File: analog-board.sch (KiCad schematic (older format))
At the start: 488 parts, among them J1 AC IN, J2 OUT, J3 CONN_20X2, P2 CONN_01X02, Q1 2N3906, Q10 2N3906, Q11 2N3906, Q12 2N3906, Q13 2N3906, Q14 2N3906, Q15 2N3906, Q16 2N3906, Q17 NPN, Q18 NPN, Q19 J111, Q2 2N3906, Q20 2N3906, Q3 2N3906, Q4 2N3906, Q5 2N3906, Q6 BCM857BS, Q7 2N3906, Q8 2N3906, Q9 2N3906, U1 LM13700, U10 ADR01, U11 DG212B, U12 DG212B, U13 DG408, U14 DG408, U15 TL072-, U16 DG408, U17 DG408, U18 LM13700, U19 LM13700, U2 LM13700, U21 TL072-, U22 TL074-, U23 TL074-, U24 TL074-, U25 TL074-, U26 TL072-, U27 TL074-, U28 TL074-, U29 LM13700, U3 LM13700, U30 LM13700, U31 TL074-, U32 LM13700, U33 TL074-, U34 TL074-, U35 TL074-, U36 74LV573, U38 0 - 10V, U39 TL074-, U4 DG212B, U40 DG419, U41 0 - 10V, U42 10 - 0V, U43 LM7812, U44 LM7912, U45 DG408, U46 7805, U5 TL074-, U6 AD5556, U7 TL072-, U8 TL074-, U9 AD8672

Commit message: added 74HC75 LFO demux latch and fixed 7912 negative voltage regulator pin out. Not finished routing new changes
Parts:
- added U20: 74HC75, symbol 74HC75
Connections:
- net +12V: now also U45.2 (EN)
- net +5V: now also U20.5 (VCC)
- net DB0: now also U20.2 (D0); no longer U45.1 (A0)
- net DB1: now also U20.3 (D1); no longer U45.16 (A1)
- net DB2: now also U20.6 (D2); no longer U45.15 (A2)
- net GND: now also U20.12 (GND), U20.7 (D3)
- net LFO DMUX EN: now also U20.13 (E01), U20.4 (E23); no longer U45.2 (EN)
- new net: U20.16 (Q0), U45.1 (A0)
- new net: U20.10 (Q2), U45.15 (A2)
- new net: U20.15 (Q1), U45.16 (A1)
- no-connect marks 12 -> 17
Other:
- note added: "*"
- note added: "*NOTE: 7912 and 7812 DO NOT HAVE THE SAME PIN OUT!"
- note added: "R181 changed to 750K \nand R180 changed to\n10K on first prototype\nto get 10V-pp noise signal"
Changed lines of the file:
@@
 LIBS:MySynthParts
 LIBS:analog-board-cache
-EELAYER 24 0
+EELAYER 25 0
 EELAYER END
 $Descr E 44000 34000
@@
 	-1   0    0    -1
 $EndComp
-Text GLabel 42300 4200 2    40   Input ~ 0
+Text GLabel 40850 7500 0    40   Input ~ 0
 DB0
-Text GLabel 42300 4300 2    40   Input ~ 0
+Text GLabel 40850 7600 0    40   Input ~ 0
 DB1
-Text GLabel 42300 4050 2    40   Input ~ 0
+Text GLabel 40800 8000 0    40   Input ~ 0
 LFO DMUX EN
 $Comp
@@
 Text Notes 40500 3500 0    60   ~ 0
 TRI
-Text GLabel 42300 4400 2    40   Input ~ 0
+Text GLabel 40850 7700 0    40   Input ~ 0
 DB2
 Text Notes 31400 1300 0    100  ~ 0
@@
 	35850 16500 35950 16500
 Wire Wire Line
-	42300 4200 42200 4200
+	42200 4200 42550 4200
 Wire Wire Line
-	42300 4300 42200 4300
+	42200 4300 42700 4300
 Wire Wire Line
-	42200 4050 42300 4050
+	42200 4050 42700 4050
 Wire Wire Line
 	42200 3500 42350 3500
@@
 	42200 4600 42200 5200
 Wire Wire Line
-	42200 4400 42300 4400
+	42200 4400 42850 4400
 Wire Notes Line
 	31350 1100 31350 9250
@@
 Text Notes 13850 26600 0    100  ~ 0
 CVs are unipolar signals. Should \nV- be connected to GND instead?
+Text Notes 36650 5950 0    60   ~ 0
+R181 changed to 750K \nand R180 changed to\n10K on first prototype\nto get 10V-pp noise signal
+$Comp
+L 74HC75 U20
+U 1 1 5560FCFF
+P 41550 7850
+F 0 "U20" H 41900 8300 60  0000 C CNN
+F 1 "74HC75" H 41550 7850 60  0000 C CNN
+F 2 "" H 41550 7850 60  0000 C CNN
+F 3 "" H 41550 7850 60  0000 C CNN
+	1    41550 7850
+	1    0    0    -1
+$EndComp
+$Comp
+L GND_E #PWR0337
+U 1 1 556207D0
+P 41550 8550
+F 0 "#PWR0337" V 41550 8550 30  0001 C CNN
+F 1 "GND_E" H 41550 8480 30  0001 C CNN
+F 2 "~" H 41550 8550 60  0000 C CNN
+F 3 "~" H 41550 8550 60  0000 C CNN
+	1    41550 8550
+	1    0    0    -1
+$EndComp
+Wire Wire Line
+	41550 8450 41550 8550
+$Comp
+L +5V #PWR0338
+U 1 1 55626424
+P 41550 7200
+F 0 "#PWR0338" H 41550 7300 30  0001 C CNN
+F 1 "+5V" H 41550 7450 60  0000 C TNN
+F 2 "~" H 41550 7200 60  0000 C CNN
+F 3 "~" H 41550 7200 60  0000 C CNN
+	1    41550 7200
+	1    0    0    -1
+$EndComp
+Wire Wire Line
+	41550 7200 41550 7250
+Wire Wire Line
+	40800 8000 40850 8000
+Wire Wire Line
+	40850 8000 40850 8100
+$Comp
+L +12V #PWR0339
+U 1 1 55635D24
+P 42700 3850
+F 0 "#PWR0339" H 42700 3950 30  0001 C CNN
+F 1 "+12V" H 42700 4050 60  0000 C CNN
+F 2 "~" H 42700 3850 60  0000 C CNN
+F 3 "~" H 42700 3850 60  0000 C CNN
+	1    42700 3850
+	1    0    0    -1
+$EndComp
+Wire Wire Line
+	42700 4050 42700 3850
+NoConn ~ 42250 7900
+NoConn ~ 42250 8000
+NoConn ~ 42250 8100
+NoConn ~ 42250 8200
+Wire Wire Line
+	42550 4200 42550 7500
+Wire Wire Line
+	42550 7500 42250 7500
+Wire Wire Line
+	42250 7600 42700 7600
+Wire Wire Line
+	42700 7600 42700 4300
+Wire Wire Line
+	42850 4400 42850 7700
+Wire Wire Line
+	42850 7700 42250 7700
+$Comp
+L GND_E #PWR0340
+U 1 1 5564046E
+P 40200 7900
+F 0 "#PWR0340" V 40200 7900 30  0001 C CNN
+F 1 "GND_E" H 40200 7830 30  0001 C CNN
+F 2 "~" H 40200 7900 60  0000 C CNN
+F 3 "~" H 40200 7900 60  0000 C CNN
+	1    40200 7900
+	1    0    0    -1
+$EndComp
+Wire Wire Line
+	40850 7800 40200 7800
+Wire Wire Line
+	40200 7800 40200 7900
+NoConn ~ 42250 7800
+Text Notes 38300 25600 0    60   ~ 0
+*NOTE: 7912 and 7812 DO NOT HAVE THE SAME PIN OUT!
+Text Notes 39550 25050 0    60   ~ 0
+*
 $EndSCHEMATC

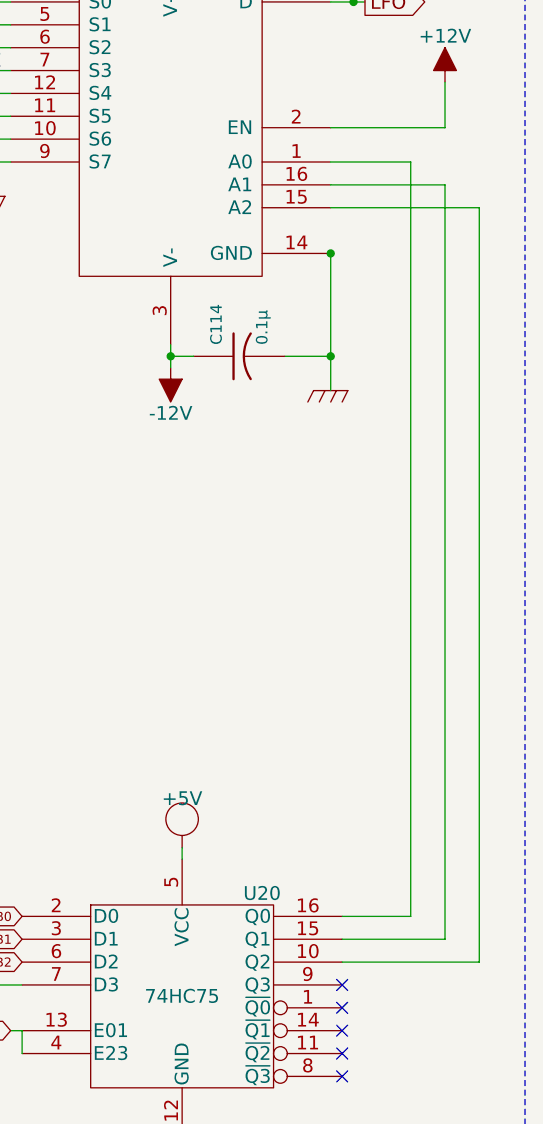
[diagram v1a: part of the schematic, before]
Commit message: 74LC75 quad latch added and routed. Probably need to change layout of S&H circuit as there is droop
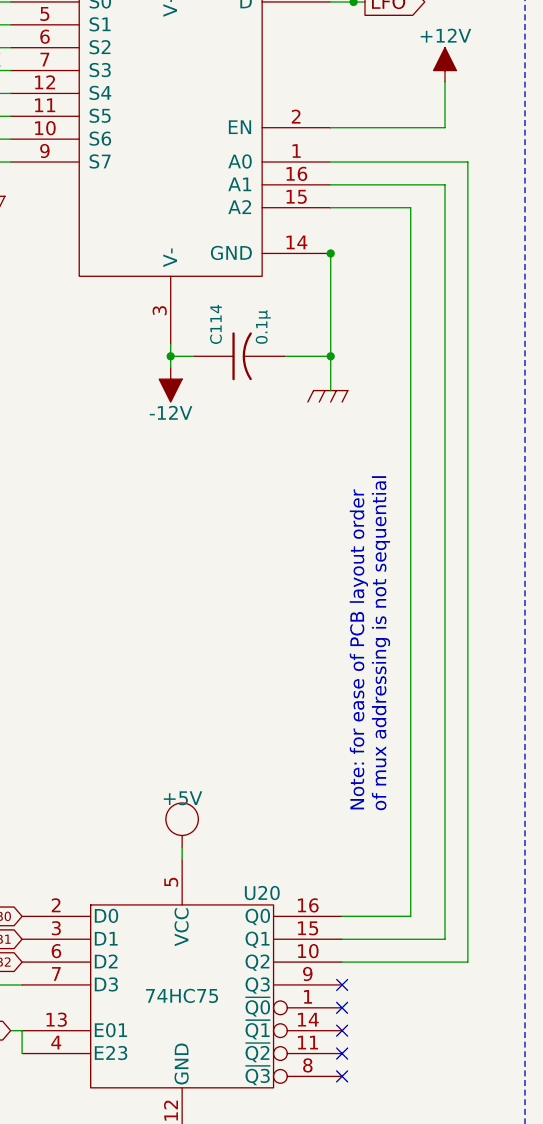
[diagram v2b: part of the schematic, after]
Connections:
- net at U45.1 (A0): now also U20.10 (Q2); no longer U20.16 (Q0)
- net at U45.15 (A2): now also U20.16 (Q0); no longer U20.10 (Q2)
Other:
- note added: "Note: for ease of PCB layout order\nof mux addressing is not sequential"
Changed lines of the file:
@@
 	35850 16500 35950 16500
 Wire Wire Line
-	42200 4200 42550 4200
+	42200 4200 42800 4200
 Wire Wire Line
 	42200 4300 42700 4300
@@
 	42200 4600 42200 5200
 Wire Wire Line
-	42200 4400 42850 4400
+	42200 4400 42550 4400
 Wire Notes Line
 	31350 1100 31350 9250
@@
 NoConn ~ 42250 8200
 Wire Wire Line
-	42550 4200 42550 7500
-Wire Wire Line
 	42550 7500 42250 7500
 Wire Wire Line
@@
 Wire Wire Line
 	42700 7600 42700 4300
-Wire Wire Line
-	42850 4400 42850 7700
-Wire Wire Line
-	42850 7700 42250 7700
 $Comp
 L GND_E #PWR0340
@@
 Text Notes 39550 25050 0    60   ~ 0
 *
+Wire Wire Line
+	42800 4200 42800 7700
+Wire Wire Line
+	42800 7700 42250 7700
+Wire Wire Line
+	42550 4400 42550 7500
+Text Notes 42450 7050 1    60   ~ 0
+Note: for ease of PCB layout order\nof mux addressing is not sequential
 $EndSCHEMATC

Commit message: added footprint note changes to schematic
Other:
- note added: "NP0 or FILM\nNeed to change to larger footprint here!"
- note added: "Need to change to\nlarger footprint here!"
- note removed: "NP0 or FILM"
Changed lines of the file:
@@
 	1    0    0    -1
 $EndComp
-Text Notes 39000 7300 0    60   ~ 0
-NP0 or FILM
+Text Notes 39000 7350 0    60   ~ 0
+NP0 or FILM\nNeed to change to larger footprint here!
 $Comp
 L GND #PWR0114
@@
 Text Notes 42450 7050 1    60   ~ 0
 Note: for ease of PCB layout order\nof mux addressing is not sequential
+Text Notes 18400 9150 0    60   ~ 0
+Need to change to\nlarger footprint here!
+Text Notes 18300 11000 0    60   ~ 0
+Need to change to\nlarger footprint here!
 $EndSCHEMATC

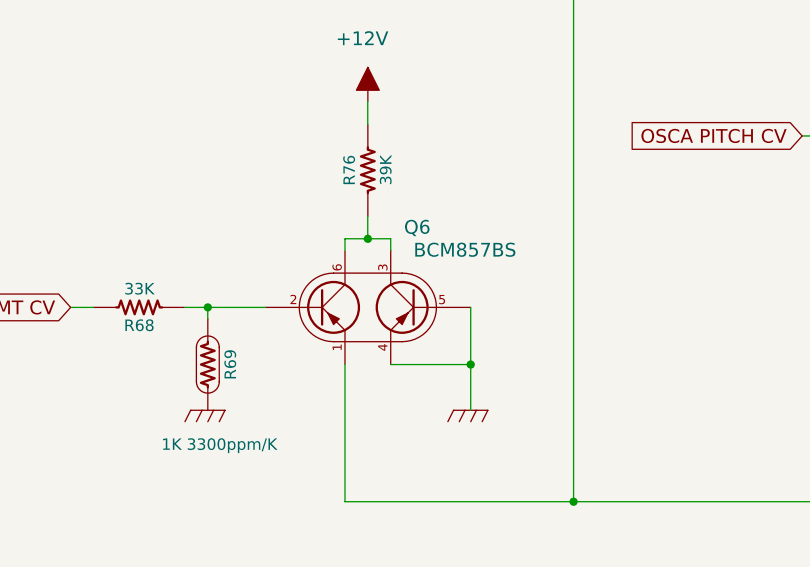
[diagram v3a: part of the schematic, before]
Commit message: fixed Q6 swap in schematic and rerouted
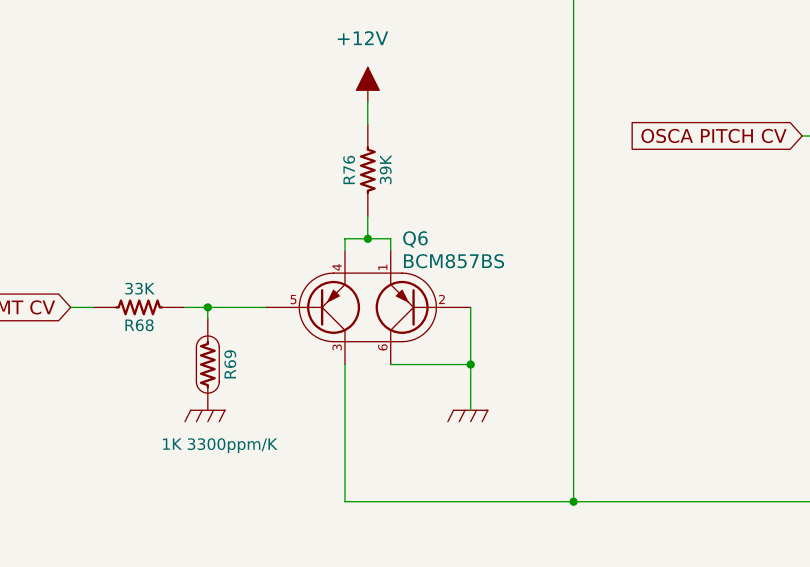
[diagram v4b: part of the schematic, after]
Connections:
- net GND: now also Q6.2 (B1), Q6.6 (C1); no longer Q6.4 (E2), Q6.5 (B2)
- net at R81.2, R84.2: now also Q6.3 (C2); no longer Q6.1 (E1)
- net at R68.1, R69.1: now also Q6.5 (B2); no longer Q6.2 (B1)
- new net: Q6.1 (E1), Q6.4 (E2), R76.1
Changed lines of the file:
@@
 U 1 1 5453F478
 P 14150 8900
-F 0 "Q6" H 14425 9250 60  0000 R CNN
-F 1 "BCM857BS" H 14800 9150 60  0000 R CNN
+F 0 "Q6" H 14000 8600 60  0000 R CNN
+F 1 "BCM857BS" H 14000 8700 60  0000 R CNN
 F 2 "~" H 13950 8900 60  0000 C CNN
 F 3 "~" H 13950 8900 60  0000 C CNN
 	1    14150 8900
-	1    0    0    -1
+	-1   0    0    1
 $EndComp
 $Comp

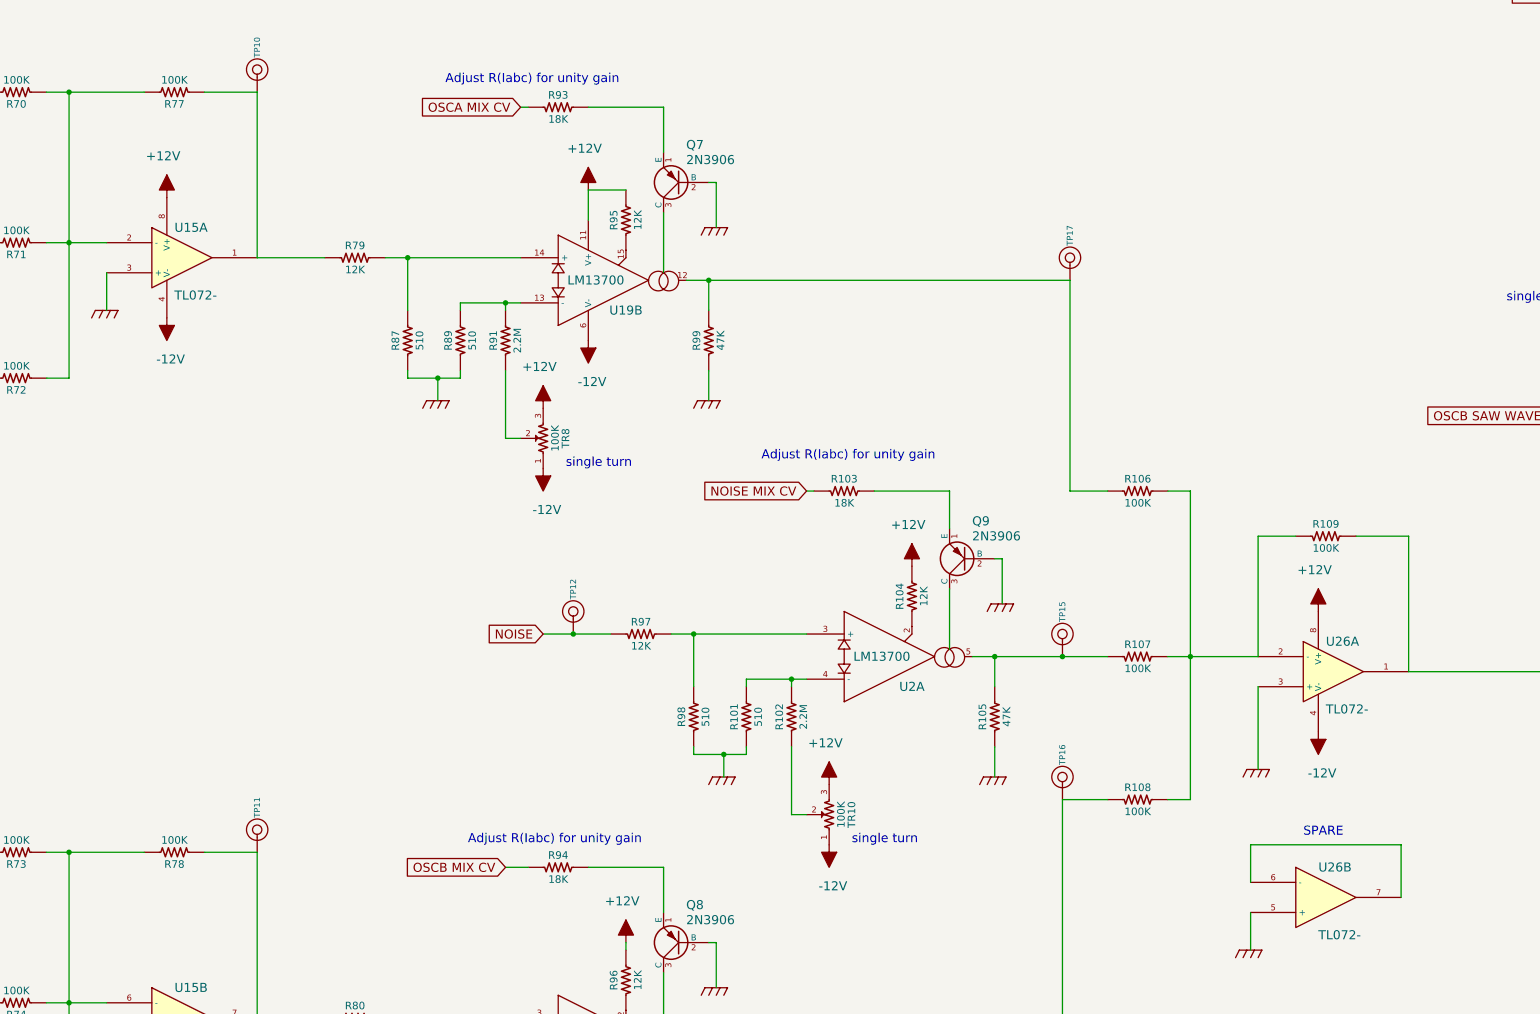
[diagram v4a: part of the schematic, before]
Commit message: fixed R73 and R78 label swap on PCB silkscreen. Added notes to schematic about changing feedback resistor value to reduce gain of waveform and summing mixers
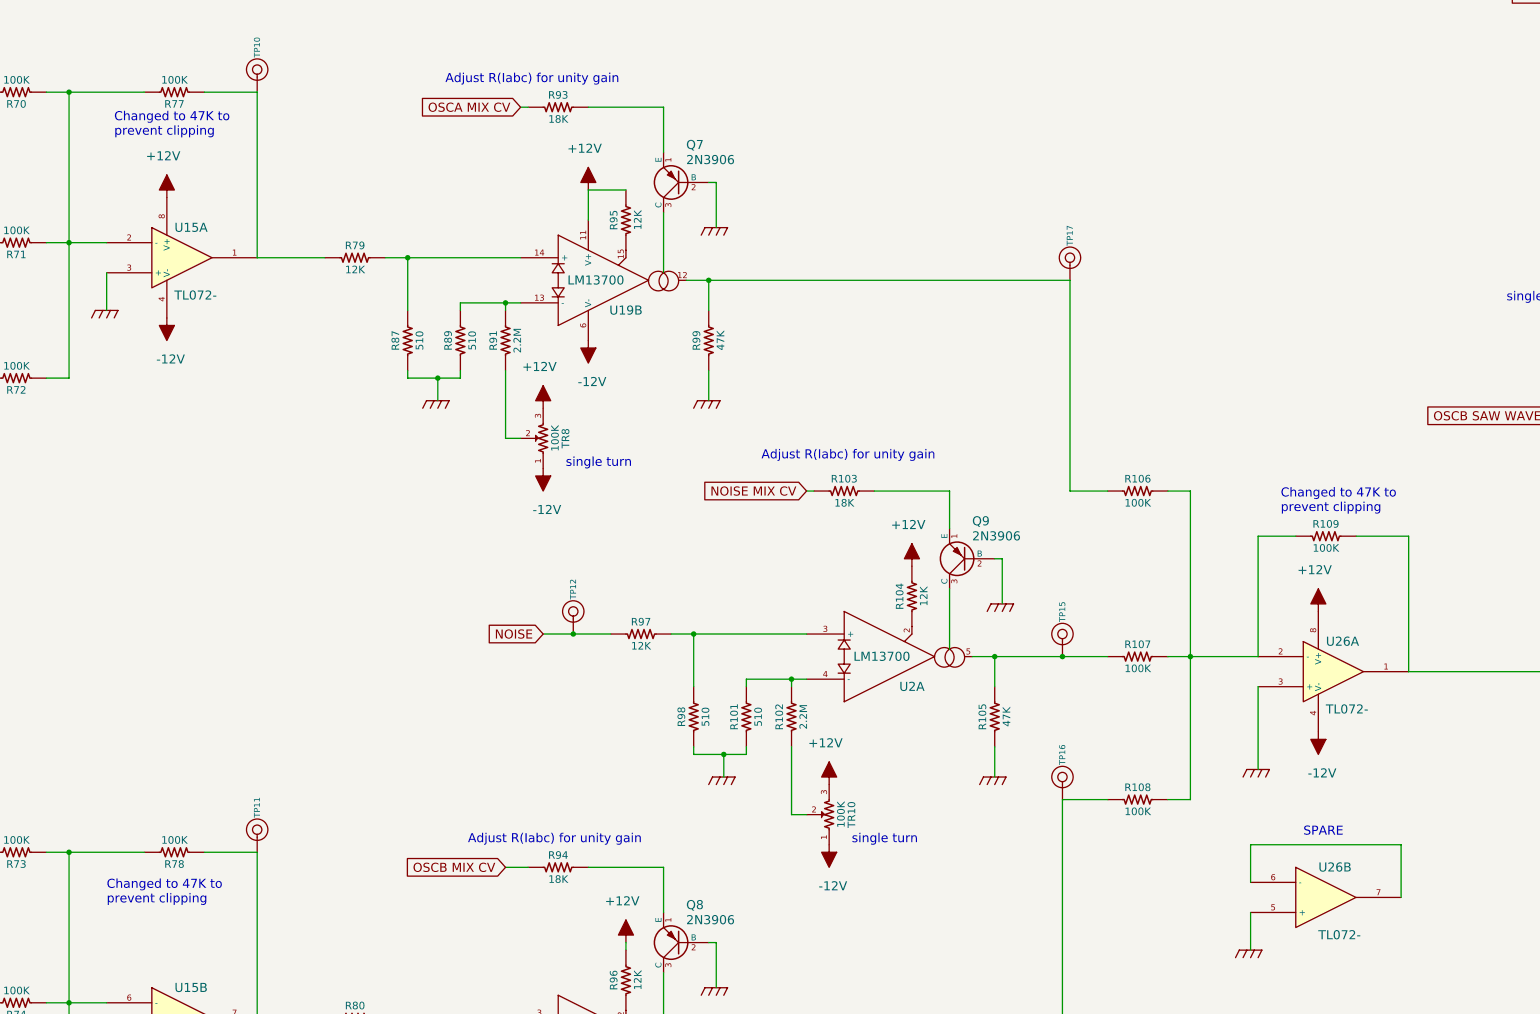
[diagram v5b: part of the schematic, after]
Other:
- note added: "Changed to 47K to\nprevent clipping"
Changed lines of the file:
@@
 Text Notes 18300 11000 0    60   ~ 0
 Need to change to\nlarger footprint here!
+Text Notes 14600 13800 0    60   ~ 0
+Changed to 47K to\nprevent clipping
+Text Notes 14550 18900 0    60   ~ 0
+Changed to 47K to\nprevent clipping
+Text Notes 22350 16300 0    60   ~ 0
+Changed to 47K to\nprevent clipping
 $EndSCHEMATC

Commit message: added some notes to schematic about capacitor packages and values based on evalutation of v1.0 analog board
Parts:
- added R? (x2): 220K, symbol R_US
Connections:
- net -12V: now also R?.1, R?.1
- net at R43.1, R44.1, R45.1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: now also R?.2
- net at R46.1, R47.1, R48.1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: now also R?.2
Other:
- note added: "*NOTE: C47 and C48 values: need\nto experiment more with C47 and \nC48 values. Change to dual\nfootprint 0805 and TH."
- note added: "*NOTE: jumper 1K output resistor\non EG2 module; it forms a divider \nwith input resistors to EG2 \nmodulation depth VCAs"
- note added: "J2 pins mixed up, results in \noutput being shorted to ground!"
- note added: "bias PWM MOD \nCVs down -5V"
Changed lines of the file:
@@
 	32400 2300 33400 2300
 Wire Wire Line
-	7000 15700 7400 15700
+	6450 15700 7400 15700
 Wire Wire Line
 	6250 14200 7000 14200
@@
 	6150 23100 5700 23100
 Wire Wire Line
-	7150 22100 7150 23900
+	7150 22100 7150 24350
 Wire Wire Line
 	2950 19800 2950 24400
@@
 Text Notes 22350 16300 0    60   ~ 0
 Changed to 47K to\nprevent clipping
+$Comp
+L R_US R?
+U 1 1 5576A3F2
+P 6450 15950
+F 0 "R?" V 6530 15950 50  0000 C CNN
+F 1 "220K" V 6370 15950 50  0000 C CNN
+F 2 "" H 6450 15950 60  0000 C CNN
+F 3 "" H 6450 15950 60  0000 C CNN
+	1    6450 15950
+	-1   0    0    1
+$EndComp
+$Comp
+L -12V #PWR?
+U 1 1 5576C921
+P 6450 16200
+F 0 "#PWR?" H 6450 16300 30  0001 C CNN
+F 1 "-12V" H 6425 16475 60  0000 C CNN
+F 2 "~" H 6450 16200 60  0000 C CNN
+F 3 "~" H 6450 16200 60  0000 C CNN
+	1    6450 16200
+	-1   0    0    1
+$EndComp
+Wire Wire Line
+	6450 15750 6450 15700
+Wire Wire Line
+	6450 16150 6450 16200
+Text Notes 6250 15600 0    60   ~ 0
+bias PWM MOD \nCVs down -5V
+Wire Wire Line
+	7150 24350 6200 24350
+$Comp
+L R_US R?
+U 1 1 55777063
+P 6200 24600
+F 0 "R?" V 6280 24600 50  0000 C CNN
+F 1 "220K" V 6120 24600 50  0000 C CNN
+F 2 "" H 6200 24600 60  0000 C CNN
+F 3 "" H 6200 24600 60  0000 C CNN
+	1    6200 24600
+	-1   0    0    1
+$EndComp
+$Comp
+L -12V #PWR?
+U 1 1 55777069
+P 6200 24850
+F 0 "#PWR?" H 6200 24950 30  0001 C CNN
+F 1 "-12V" H 6175 25125 60  0000 C CNN
+F 2 "~" H 6200 24850 60  0000 C CNN
+F 3 "~" H 6200 24850 60  0000 C CNN
+	1    6200 24850
+	-1   0    0    1
+$EndComp
+Wire Wire Line
+	6200 24350 6200 24400
+Wire Wire Line
+	6200 24800 6200 24850
+Text Notes 6000 24250 0    60   ~ 0
+bias PWM MOD \nCVs down -5V
+Connection ~ 7150 23900
+Text Notes 40700 16450 0    60   ~ 0
+J2 pins mixed up, results in \noutput being shorted to ground!
+Text Notes 35600 30650 0    60   ~ 0
+*NOTE: jumper 1K output resistor\non EG2 module; it forms a divider \nwith input resistors to EG2 \nmodulation depth VCAs
+Text Notes 16450 11100 0    60   ~ 0
+*NOTE: C47 and C48 values: need\nto experiment more with C47 and \nC48 values. Change to dual\nfootprint 0805 and TH.
 $EndSCHEMATC
